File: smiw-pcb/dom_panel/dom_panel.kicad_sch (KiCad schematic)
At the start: 4 parts, among them J1 4-1734839-5, U1 ESP32-S3-DEVKITC-1-N8R8, U2 SN74AVC16T245DGGR, U3 SN74AVC16T245DGGR

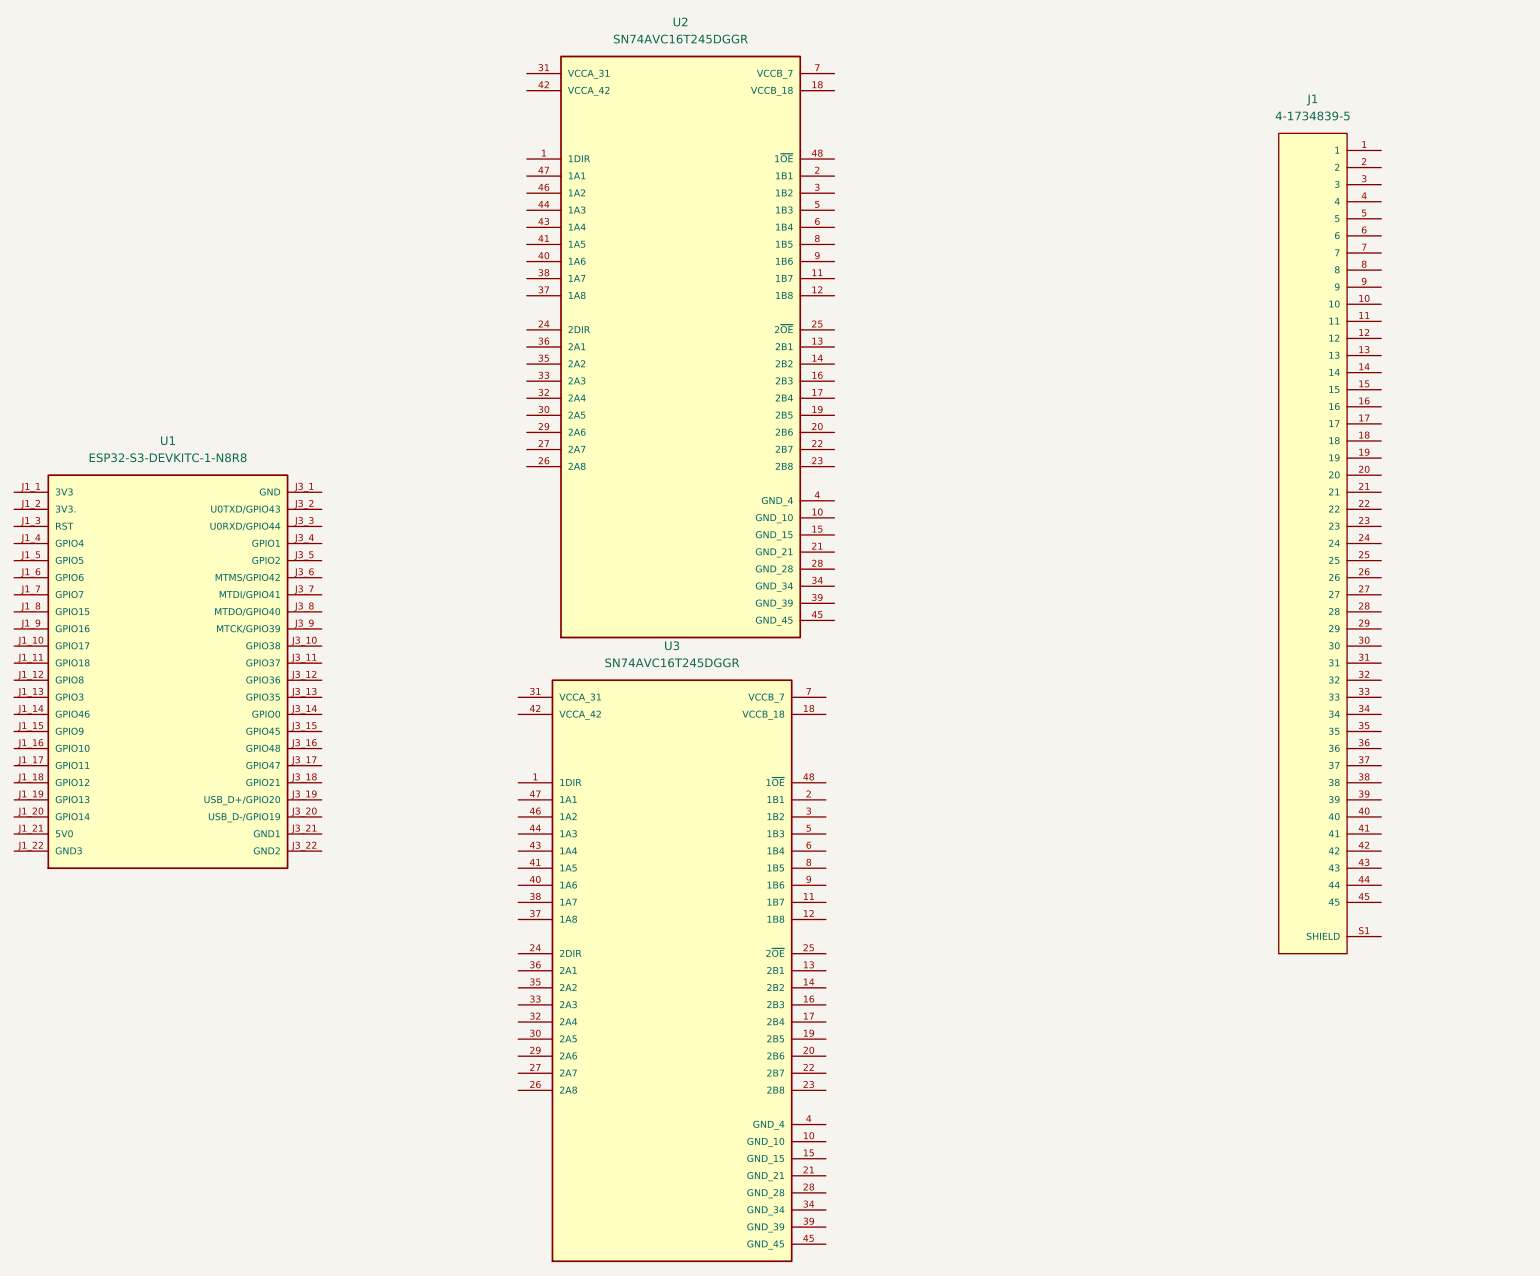
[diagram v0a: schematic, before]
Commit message: Added basic power lines
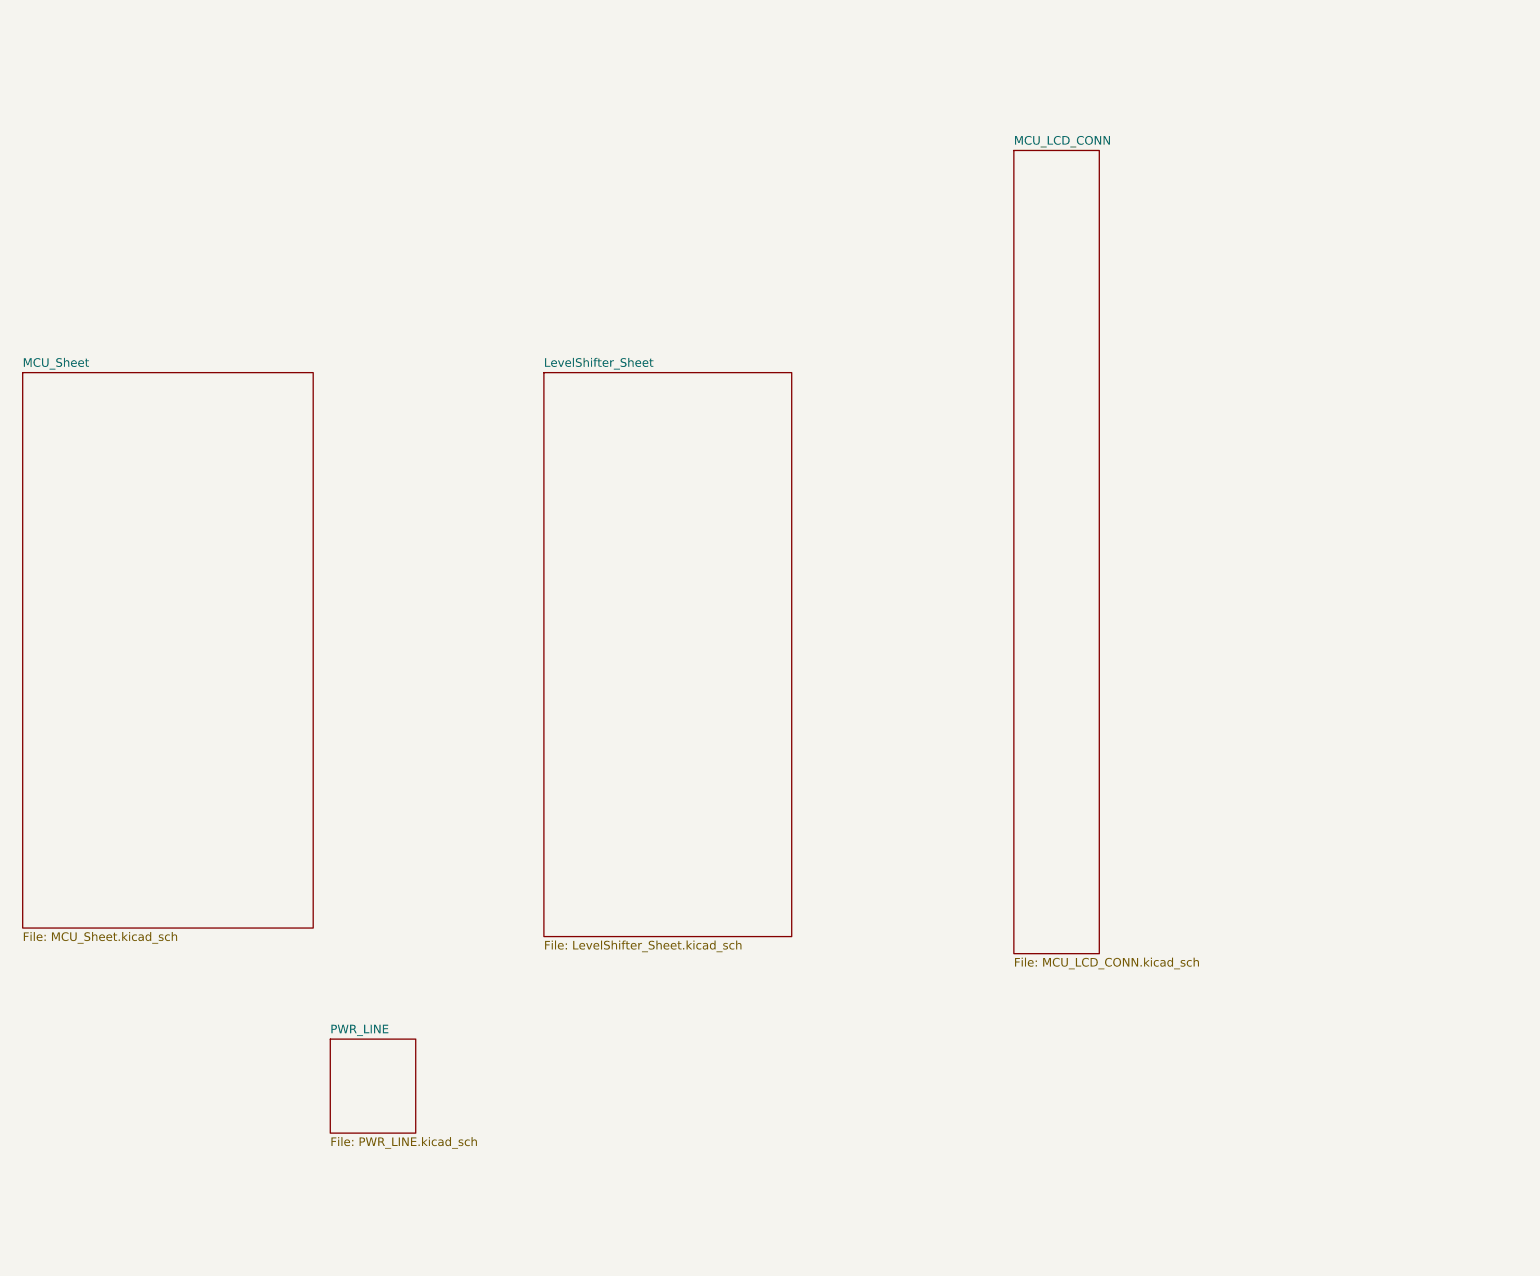
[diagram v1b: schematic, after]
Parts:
- removed J1: 4-1734839-5, 4-1734839-5:TE_4-1734839-5, symbol FPC-CON-45PIN-0.5MM:4-1734839-5
- removed U1: ESP32-S3-DEVKITC-1-N8R8, ESP32-S3-DEVKITC-1-N8R8:ESP32-S3-DEVKITC-1-N8R8, symbol ESP32-S3-DEVKITC-1-N8R8:ESP32-S3-DEVKITC-1-N8R8
- removed U2, U3: SN74AVC16T245DGGR, SN74AVC16T245DGGR:SOP50P810X120-48N, symbol SN74AVC16T245DGGR:SN74AVC16T245DGGR
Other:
- added sheet LevelShifter_Sheet (LevelShifter_Sheet.kicad_sch)
- added sheet MCU_LCD_CONN (MCU_LCD_CONN.kicad_sch)
- added sheet MCU_Sheet (MCU_Sheet.kicad_sch)
- added sheet PWR_LINE (PWR_LINE.kicad_sch)

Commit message: cos
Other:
- added sheet LORA_SHEET (LORA_SHEET.kicad_sch)
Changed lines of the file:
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@@
 	(paper "A4")
 	(sheet
-		(at 106.68 64.77)
+		(at 147.574 20.066)
 		(size 36.83 83.82)
 		(exclude_from_sim no)
@@
 		)
 		(property "Sheetname" "LevelShifter_Sheet"
-			(at 106.68 64.0584 0)
+			(at 147.574 19.3544 0)
 			(effects
 				(font
@@
 		)
 		(property "Sheetfile" "LevelShifter_Sheet.kicad_sch"
-			(at 106.68 149.1746 0)
+			(at 147.574 104.4706 0)
 			(effects
 				(font
@@
 	)
 	(sheet
-		(at 74.93 163.83)
+		(at 151.384 136.652)
+		(size 23.114 16.51)
+		(exclude_from_sim no)
+		(in_bom yes)
+		(on_board yes)
+		(dnp no)
+		(fields_autoplaced yes)
+		(stroke
+			(width 0.1524)
+			(type solid)
+		)
+		(fill
+			(color 0 0 0 0.0000)
+		)
+		(property "Sheetname" "LORA_SHEET"
+			(at 151.384 135.9404 0)
+			(effects
+				(font
+					(size 1.27 1.27)
+				)
+				(justify left bottom)
+			)
+		)
+		(property "Sheetfile" "LORA_SHEET.kicad_sch"
+			(at 151.384 153.7466 0)
+			(effects
+				(font
+					(size 1.27 1.27)
+				)
+				(justify left top)
+			)
+		)
+		(instances
+			(project "dom_panel"
+				(path "/8fbd3732-812c-4333-8351-7e7df938a7a4"
+					(page "6")
+				)
+			)
+		)
+	)
+	(sheet
+		(at 113.538 172.212)
 		(size 12.7 13.97)
 		(exclude_from_sim no)
@@
 		)
 		(property "Sheetname" "PWR_LINE"
-			(at 74.93 163.1184 0)
+			(at 113.538 171.5004 0)
 			(effects
 				(font
@@
 		)
 		(property "Sheetfile" "PWR_LINE.kicad_sch"
-			(at 74.93 178.3846 0)
+			(at 113.538 186.7666 0)
 			(effects
 				(font
@@
 	)
 	(sheet
-		(at 176.53 31.75)
+		(at 217.17 16.51)
 		(size 12.7 119.38)
 		(exclude_from_sim no)
@@
 		)
 		(property "Sheetname" "MCU_LCD_CONN"
-			(at 176.53 31.0384 0)
+			(at 217.17 15.7984 0)
 			(effects
 				(font
@@
 		)
 		(property "Sheetfile" "MCU_LCD_CONN.kicad_sch"
-			(at 176.53 151.7146 0)
+			(at 217.17 136.4746 0)
 			(effects
 				(font
@@
 	)
 	(sheet
-		(at 29.21 64.77)
+		(at 59.436 64.262)
 		(size 43.18 82.55)
 		(exclude_from_sim no)
@@
 		)
 		(property "Sheetname" "MCU_Sheet"
-			(at 29.21 64.0584 0)
+			(at 59.436 63.5504 0)
 			(effects
 				(font
@@
 		)
 		(property "Sheetfile" "MCU_Sheet.kicad_sch"
-			(at 29.21 147.9046 0)
+			(at 59.436 147.3966 0)
 			(effects
 				(font
